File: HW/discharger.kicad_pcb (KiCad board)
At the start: 2 copper layers, 53.9 x 33.4 mm, 15 parts, among them J1 Conn_01x04_Male, J2 Conn_01x02_Male, Q1 IRFFR220N, U1 MCP4725, U2 OP07, U3 OP07, U4 INA219

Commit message: Add files via upload
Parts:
- removed U3: OP07, Housings_DIP:DIP-8_W7.62mm_Socket_LongPads
- removed U4: INA219, TO_SOT_Packages_SMD:SOT-23-8_Handsoldering
- added 1U1: 0,1U, Capacitors_SMD:C_0805_HandSoldering, F.Cu at (333.5, 75.7)
- added 1U2: 0,1U, Capacitors_SMD:C_0805_HandSoldering, F.Cu at (325.8, 84.5)
- added C10: 100n, Capacitors_SMD:C_0805_HandSoldering, F.Cu at (228.1, 115.7)
- added C11: 100n, Capacitors_SMD:C_0805_HandSoldering, F.Cu at (233.1, 115.7)
- added C12: 100n, Capacitors_SMD:C_0805_HandSoldering, F.Cu at (290.9, 72.5)
- added C13: C, Capacitors_SMD:C_0805_HandSoldering, F.Cu at (265.3, 94.9)
- added C14: C, Capacitors_SMD:C_0805_HandSoldering, F.Cu at (283.9, 76.8)
- added C15: 100n, Capacitors_SMD:C_0805_HandSoldering, F.Cu at (270.2, 97.9)
- added C18: 100n, Capacitors_SMD:C_0805_HandSoldering, F.Cu at (265.3, 100.4)
- added C19: C, Capacitors_SMD:C_0805_HandSoldering, F.Cu at (288.8, 78.0)
- added C20: 0,1u, Capacitors_SMD:C_0805_HandSoldering, F.Cu at (344.8, 65.8)
- added C21: 10uF, Capacitors_Tantalum_SMD:CP_Tantalum_Case-C_EIA-6032-28_Hand, F.Cu at (329.7, 67.4)
- added C22: 0,1U, Capacitors_SMD:C_0805_HandSoldering, F.Cu at (349.7, 65.8)
- added C23: 22pf, Capacitors_SMD:C_0805_HandSoldering, F.Cu at (344.8, 71.3)
- added C24: 22pf, Capacitors_SMD:C_0805_HandSoldering, F.Cu at (330.7, 84.5)
- added C25: 100nF, Capacitors_SMD:C_0805_HandSoldering, F.Cu at (236.7, 126.4)
- added C26: 100nF, Capacitors_SMD:C_0805_HandSoldering, F.Cu at (253.4, 128.4)
- added C27: 100nF, Capacitors_SMD:C_0805_HandSoldering, F.Cu at (242.1, 140.2)
- added C7: C, Capacitors_SMD:C_0805_HandSoldering, F.Cu at (305.2, 119.7)
- added C8: C, Capacitors_SMD:C_0805_HandSoldering, F.Cu at (316.0, 102.2)
- added C9: 100n, Capacitors_SMD:C_0805_HandSoldering, F.Cu at (242.1, 88.8)
- added D1: LED1, LEDs:LED_D5.0mm-4, F.Cu at (317.9, 82.3)
- added D2: LED2, LEDs:LED_D5.0mm-4, F.Cu at (325.7, 76.7)
- added D3: LED3, LEDs:LED_D5.0mm-4, F.Cu at (336.9, 68.0)
- added FTDI1: FTDI, Pin_Headers:Pin_Header_Straight_1x06_Pitch2.54mm, F.Cu at (299.2, 80.5)
- added ISP1: ISP-header, Pin_Headers:Pin_Header_Straight_2x03_Pitch2.54mm, F.Cu at (310.5, 89.6)
- added J3: Batt1, Connectors_Terminal_Blocks:TerminalBlock_bornier-2_P5.08mm, F.Cu at (210.7, 127.4)
- added J4: Batt1, Connectors_Terminal_Blocks:TerminalBlock_bornier-2_P5.08mm, F.Cu at (204.6, 95.5)
- added JP1: Jumper, Pin_Headers:Pin_Header_Straight_1x03_Pitch2.54mm, F.Cu at (304.3, 89.6)
- added Q2: IRFFR220N, TO_SOT_Packages_SMD:TO-252-2, F.Cu at (192.4, 130.1)
- added Q3: IRFFR220N, TO_SOT_Packages_SMD:TO-252-2, F.Cu at (180.5, 103.4)
- added Q4: FS8205, TO_SOT_Packages_SMD:SOT-23-6_Handsoldering, F.Cu at (178.2, 67.1)
- added Q5: FS8205, TO_SOT_Packages_SMD:SOT-23-6_Handsoldering, F.Cu at (207.7, 118.6)
- added Q6: FS8205, TO_SOT_Packages_SMD:SOT-23-6_Handsoldering, F.Cu at (179.2, 73.7)
- added R10: 1K, Resistors_SMD:R_0805_HandSoldering, F.Cu at (349.8, 71.3)
- added R11: 1K, Resistors_SMD:R_0805_HandSoldering, F.Cu at (338.6, 75.7)
- added R12: 100R, Resistors_SMD:R_0805_HandSoldering, F.Cu at (244.5, 123.4)
- added R13: 100R, Resistors_SMD:R_0805_HandSoldering, F.Cu at (252.4, 143.3)
- added R14: 1K, Resistors_SMD:R_0805_HandSoldering, F.Cu at (242.1, 136.1)
- added R15: 1K, Resistors_SMD:R_0805_HandSoldering, F.Cu at (252.4, 137.8)
- added R16: 100R, Resistors_SMD:R_0805_HandSoldering, F.Cu at (247.2, 143.3)
- added R17: 1K, Resistors_SMD:R_0805_HandSoldering, F.Cu at (244.4, 147.3)
- added R18: R, Resistors_SMD:R_0805_HandSoldering, F.Cu at (343.7, 82.3)
- added R19: R, Resistors_SMD:R_0805_HandSoldering, F.Cu at (338.6, 81.2)
- added R20: R, Resistors_SMD:R_0805_HandSoldering, F.Cu at (355.0, 71.2)
- added R21: R, Resistors_SMD:R_0805_HandSoldering, F.Cu at (336.6, 86.7)
- added R22: R, Resistors_SMD:R_0805_HandSoldering, F.Cu at (349.8, 76.8)
- added R23: R, Resistors_SMD:R_0805_HandSoldering, F.Cu at (326.3, 95.5)
- added R24: R, Resistors_SMD:R_0805_HandSoldering, F.Cu at (331.4, 90.0)
- added R25: R, Resistors_SMD:R_0805_HandSoldering, F.Cu at (343.7, 76.8)
- added R26: R, Resistors_SMD:R_0805_HandSoldering, F.Cu at (354.8, 65.7)
- added R3: 0,01R, Resistors_SMD:R_2512_HandSoldering, F.Cu at (194.5, 90.3)
- added R4: 10R, Resistors_THT:R_Axial_DIN0414_L11.9mm_D4.5mm_P15.24mm_Horizontal, F.Cu at (148.6, 109.6)
- added R5: 0,01R, Resistors_SMD:R_2512_HandSoldering, F.Cu at (202.1, 129.7)
- added R6: 10R, Resistors_THT:R_Axial_DIN0414_L11.9mm_D4.5mm_P15.24mm_Horizontal, F.Cu at (184.4, 132.8)
- added R7: 0,01R, Resistors_SMD:R_2512_HandSoldering, F.Cu at (194.3, 100.9)
- added R8: 10R, Resistors_THT:R_Axial_DIN0414_L11.9mm_D4.5mm_P15.24mm_Horizontal, F.Cu at (137.9, 124.8)
- added R9: 10K, Resistors_SMD:R_0805_HandSoldering, F.Cu at (326.3, 90.0)
- added TP3: TEST, Pin_Headers:Pin_Header_Straight_1x01_Pitch2.54mm, F.Cu at (243.8, 45.9)
- added U12: OP07, Housings_DIP:DIP-8_W7.62mm_Socket_LongPads, F.Cu at (248.9, 80.7)
- added U13: INA219, TO_SOT_Packages_SMD:SOT-23-8_Handsoldering, F.Cu at (126.5, 81.6)
- added U14: ATMEGA328P-AU-Arduino, Housings_QFP:TQFP-32_7x7mm_Pitch0.8mm, F.Cu at (306.9, 70.1)
- added U15: DW01-P, TO_SOT_Packages_SMD:SOT-23-6_Handsoldering, F.Cu at (162.4, 66.6)
- added U16: DW01-P, TO_SOT_Packages_SMD:SOT-23-6_Handsoldering, F.Cu at (203.3, 118.5)
- added U17: DW01-P, TO_SOT_Packages_SMD:SOT-23-6_Handsoldering, F.Cu at (169.2, 66.4)
- added U6: OP07, Housings_DIP:DIP-8_W7.62mm_Socket_LongPads, F.Cu at (219.1, 83.7)
- added U7: OP07, Housings_DIP:DIP-8_W7.62mm_Socket_LongPads, F.Cu at (224.5, 67.3)
- added U8: INA219, TO_SOT_Packages_SMD:SOT-23-8_Handsoldering, F.Cu at (126.5, 94.5)
- added U9: INA219, TO_SOT_Packages_SMD:SOT-23-8_Handsoldering, F.Cu at (126.4, 88.2)
- added Y1: 8MHZ, Crystals:Crystal_HC18-U_Vertical, F.Cu at (305.2, 81.7)
- C1: value C -> 10uF; footprint Capacitors_SMD:C_0805_HandSoldering -> Capacitors_Tantalum_SMD:CP_Tantalum_Case-C_EIA-6032-28_Hand
- C2: value C -> 2uF
- C3: value C -> 100uF; footprint Capacitors_SMD:C_0805_HandSoldering -> Capacitors_THT:CP_Radial_D6.3mm_P2.50mm
- C4: value C -> 2nF
- J1: value Conn_01x04_Male -> OLED; footprint Pin_Headers:Pin_Header_Straight_1x04_Pitch2.54mm_SMD_Pin1Right -> Pin_Headers:Pin_Header_Straight_1x04_Pitch2.54mm_SMD_Pin1Left
- J2: value Conn_01x02_Male -> Batt1; footprint Pin_Headers:Pin_Header_Straight_1x02_Pitch2.54mm_SMD_Pin1Right -> Connectors_Terminal_Blocks:TerminalBlock_bornier-2_P5.08mm
- R1: value 0,01R -> 20K; footprint Resistors_SMD:R_2512_HandSoldering -> Resistors_SMD:R_0805_HandSoldering
- R2: value 10R -> 102.6K; footprint Resistors_THT:R_Axial_DIN0414_L11.9mm_D4.5mm_P15.24mm_Horizontal -> Resistors_SMD:R_0805_HandSoldering
- U1: value MCP4725 -> LT1054; footprint TO_SOT_Packages_SMD:SOT-23-6_Handsoldering -> Housings_DIP:DIP-8_W7.62mm_LongPads
- U2: value OP07 -> MCP4728; footprint Housings_DIP:DIP-8_W7.62mm_Socket_LongPads -> Housings_SSOP:MSOP-10_3x3mm_Pitch0.5mm
- moved C4 168.3 mm to (326.7, 105.4), turned to 0 degrees
- moved C1 164.3 mm to (313.6, 107.0), turned to 0 degrees
- moved C2 162.2 mm to (321.7, 110.9), turned to 0 degrees
- moved U1 145.5 mm to (298.7, 105.9), turned to 0 degrees
- moved R1 145.1 mm to (326.8, 110.9), turned to 0 degrees
- moved U2 144.3 mm to (320.0, 90.9), turned to 0 degrees
- moved C3 129.5 mm to (310.5, 116.8), turned to 0 degrees
- moved J1 128.3 mm to (320.4, 70.2), turned to 0 degrees
- moved R2 124.0 mm to (299.9, 119.6)
- moved TP1 81.8 mm to (239.1, 46.0)
- moved TP2 80.1 mm to (235.5, 46.4)
- moved J2 13.1 mm to (204.6, 84.9), turned to 270 degrees
- moved Q1 5.27 mm to (180.4, 93.7), turned to 180 degrees
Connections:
- C1 pad 1: VCC -> Net-(C1-Pad1)
- C1 pad 2: GND -> Net-(C1-Pad2)
- C3 pad 1: VCC -> GND
- C3 pad 2: GND -> -5V
- C4 pad 1: VCC -> Net-(C4-Pad1)
- C4 pad 2: GND -> -5V
- J1 pad 1: VCC -> SDA
- J1 pad 2: SDA -> SCL
- J1 pad 3: SCL -> VCC
- J2 pad 1: GND -> Net-(C25-Pad2)
- J2 pad 2: Net-(J2-Pad2) -> /Battery connections/BatteryPositive1
- R1 pad 1: Net-(J2-Pad2) -> Net-(C4-Pad1)
- R1 pad 2: Net-(Q1-Pad2) -> Net-(R1-Pad2)
- R2 pad 1: Net-(Q1-Pad3) -> Net-(C4-Pad1)
- R2 pad 2: GND -> -5V
- TP1 pad 1: Net-(TP1-Pad1) -> /Dynamic load/DAC_IN1
- TP2 pad 1: Net-(TP2-Pad1) -> /Dynamic load/DAC_IN3
- U1 pad 1: Net-(TP2-Pad1) -> Net-(C4-Pad1)
- U1 pad 2: GND -> Net-(C1-Pad1)
- U1 pad 3: VCC -> GND
- U1 pad 4: SDA -> Net-(C1-Pad2)
- U1 pad 5: SCL -> -5V
- U1 pad 6: GND -> Net-(R1-Pad2)
- U2 pad 1: (no net) -> VCC
- U2 pad 2: Net-(TP1-Pad1) -> SCL
- U2 pad 3: Net-(J2-Pad2) -> SDA
- U2 pad 6: Net-(TP1-Pad1) -> /Dynamic load/DAC_IN1
- U2 pad 7: VCC -> /Dynamic load/DAC_IN2
- U2 pad 8: (no net) -> /Dynamic load/DAC_IN3
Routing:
- net VCC: track 83.0 -> 0.00 mm
- net SDA: track 65.9 -> 0.00 mm
- net SCL: track 59.8 -> 0.00 mm
- net GND: track 46.7 -> 0.00 mm
- net Net-(J2-Pad2): track 31.2 -> 0.00 mm
- net Net-(TP2-Pad1): track 27.1 -> 0.00 mm
- net Net-(Q1-Pad3): track 26.1 -> 0.00 mm
- net Net-(Q1-Pad1): track 16.9 -> 0.00 mm
- net Net-(TP1-Pad1): track 16.1 -> 0.00 mm
- net /Battery connections/BatteryPositive3: track 0.00 -> 14.0 mm
- net Net-(Q2-Pad2): track 0.00 -> 12.5 mm
- net Net-(C26-Pad2): track 0.00 -> 12.5 mm
- net Net-(Q2-Pad3): track 0.00 -> 11.3 mm
- net Net-(Q1-Pad2): track 11.0 -> 0.00 mm
- net Net-(Q5-Pad4): track 0.00 -> 9.79 mm
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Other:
- board size 53.9 x 33.4 mm -> 96.1 x 73.7 mm

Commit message: Add files via upload
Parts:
- removed C24: 22pf, Capacitors_SMD:C_0805_HandSoldering
- removed C25, C26, C27: 100nF, Capacitors_SMD:C_0805_HandSoldering
- removed ISP1: ISP-header, Pin_Headers:Pin_Header_Straight_2x03_Pitch2.54mm
- removed U14: ATMEGA328P-AU-Arduino, Housings_QFP:TQFP-32_7x7mm_Pitch0.8mm
- removed U15, U16, U17: DW01-P, TO_SOT_Packages_SMD:SOT-23-6_Handsoldering
- added C16: 10uF, Capacitors_Tantalum_SMD:CP_Tantalum_Case-C_EIA-6032-28_Hand, B.Cu at (274.0, 109.7)
- added C17: 0,1u, Capacitors_SMD:C_0805_HandSoldering, B.Cu at (245.4, 117.2)
- added C5: 2nF, Capacitors_SMD:C_0805_HandSoldering, B.Cu at (151.1, 72.1)
- added C6: 100uF, Capacitors_THT:CP_Radial_D6.3mm_P2.50mm, F.Cu at (168.8, 70.9)
- added J5: Batt1, Connectors_Terminal_Blocks:TerminalBlock_bornier-2_P5.08mm, B.Cu at (126.9, 132.0)
- added U10: MCP4728, Housings_SSOP:MSOP-10_3x3mm_Pitch0.5mm, B.Cu at (228.8, 80.5)
- added U11: DW01-P, TO_SOT_Packages_SMD:SOT-23-6_Handsoldering, F.Cu at (132.2, 103.8)
- added U3: INA219, TO_SOT_Packages_SMD:SOT-23-8_Handsoldering, F.Cu at (145.3, 107.2)
- added U4: INA219, TO_SOT_Packages_SMD:SOT-23-8_Handsoldering, F.Cu at (144.7, 82.8)
- added U5: OP07, Housings_DIP:DIP-8_W7.62mm_Socket_LongPads, F.Cu at (175.9, 108.3)
- 1U1, 1U2, C11, C12, C15, D1, D2, D3, J3, J4, R1, R10, R11, R18, R19, R2, R20, R9, Y1: moved to B.Cu
- C1: value 10uF -> 2uF; footprint Capacitors_Tantalum_SMD:CP_Tantalum_Case-C_EIA-6032-28_Hand -> Capacitors_SMD:C_0805_HandSoldering; moved to B.Cu
- C14: value C -> 100n
- C18: value 100n -> 22pf; moved to B.Cu
- C19: value C -> 0,1U; moved to B.Cu
- C2: value 2uF -> 10uF; footprint Capacitors_SMD:C_0805_HandSoldering -> Capacitors_Tantalum_SMD:CP_Tantalum_Case-C_EIA-6032-28_Hand; moved to B.Cu
- C20: value 0,1u -> 22pf; moved to B.Cu
- C21: value 10uF -> 100nF; footprint Capacitors_Tantalum_SMD:CP_Tantalum_Case-C_EIA-6032-28_Hand -> Capacitors_SMD:C_0805_HandSoldering
- C22: value 0,1U -> 100nF
- C23: value 22pf -> 100nF
- C3: value 100uF -> 10uF; footprint Capacitors_THT:CP_Radial_D6.3mm_P2.50mm -> Capacitors_SMD:C_0805_HandSoldering; moved to B.Cu
- C4: value 2nF -> 0,1uF; moved to B.Cu
- J1: value OLED -> Vin; footprint Pin_Headers:Pin_Header_Straight_1x04_Pitch2.54mm_SMD_Pin1Left -> Connectors_Terminal_Blocks:TerminalBlock_bornier-2_P5.08mm; moved to B.Cu
- J2: value Batt1 -> OLED; footprint Connectors_Terminal_Blocks:TerminalBlock_bornier-2_P5.08mm -> Pin_Headers:Pin_Header_Straight_1x04_Pitch2.54mm_SMD_Pin1Left; moved to B.Cu
- Q4, Q5, Q6: value FS8205 -> IRF7341; footprint TO_SOT_Packages_SMD:SOT-23-6_Handsoldering -> Housings_SOIC:SO-8_5.3x6.2mm_Pitch1.27mm
- R12, R13, R16: value 100R -> R; moved to B.Cu
- R14, R15, R17: value 1K -> R; moved to B.Cu
- R21, R22, R25: value R -> 100R
- R23, R24, R26: value R -> 1K
- R4: value 10R -> 0,01R; footprint Resistors_THT:R_Axial_DIN0414_L11.9mm_D4.5mm_P15.24mm_Horizontal -> Resistors_SMD:R_2512_HandSoldering
- R5: value 0,01R -> 10R; footprint Resistors_SMD:R_2512_HandSoldering -> Resistors_THT:R_Axial_DIN0414_L11.9mm_D4.5mm_P15.24mm_Horizontal
- U1: value LT1054 -> LM2937; footprint Housings_DIP:DIP-8_W7.62mm_LongPads -> TO_SOT_Packages_SMD:SOT-223-3_TabPin2; moved to B.Cu
- U12: value OP07 -> DW01-P; footprint Housings_DIP:DIP-8_W7.62mm_Socket_LongPads -> TO_SOT_Packages_SMD:SOT-23-6_Handsoldering
- U13: value INA219 -> DW01-P; footprint TO_SOT_Packages_SMD:SOT-23-8_Handsoldering -> TO_SOT_Packages_SMD:SOT-23-6_Handsoldering
- U2: value MCP4728 -> LT1054; footprint Housings_SSOP:MSOP-10_3x3mm_Pitch0.5mm -> Housings_DIP:DIP-8_W7.62mm_LongPads
- U7: value OP07 -> INA219; footprint Housings_DIP:DIP-8_W7.62mm_Socket_LongPads -> TO_SOT_Packages_SMD:SOT-23-8_Handsoldering
- U8: value INA219 -> OP07; footprint TO_SOT_Packages_SMD:SOT-23-8_Handsoldering -> Housings_DIP:DIP-8_W7.62mm_Socket_LongPads
- U9: value INA219 -> ATMEGA328P-AU-Arduino; footprint TO_SOT_Packages_SMD:SOT-23-8_Handsoldering -> Housings_QFP:TQFP-32_7x7mm_Pitch0.8mm; moved to B.Cu
- moved R26 233.2 mm to (128.3, 121.0), turned to 90 degrees
- moved R25 228.1 mm to (122.6, 132.6), turned to 270 degrees
- moved C23 227.9 mm to (123.7, 126.7), turned to 270 degrees
- moved C22 219.2 mm to (130.8, 76.2), turned to 180 degrees
- moved R22 219.0 mm to (130.8, 73.7), turned to 180 degrees
- moved R21 206.0 mm to (130.8, 97.4), turned to 180 degrees
- moved C21 201.6 mm to (130.8, 99.9), turned to 180 degrees
- moved J1 196.1 mm to (124.3, 67.2)
- moved R24 194.8 mm to (136.9, 80.0)
- moved C4 194.2 mm to (135.6, 71.1), turned to 90 degrees
- moved R23 189.8 mm to (136.7, 103.8)
- moved R1 184.8 mm to (146.2, 72.0), turned to 90 degrees
- moved C3 176.1 mm to (140.4, 71.1), turned to 90 degrees
- moved C1 168.9 mm to (150.1, 64.8), turned to 180 degrees
- moved C8 167.4 mm to (149.5, 84.3)
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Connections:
- C1 pad 1: Net-(C1-Pad1) -> VCC
- C1 pad 2: Net-(C1-Pad2) -> GND
- C11 pad 1: VCC -> GND
- C12 pad 1: VCC -> GND
- C15 pad 1: VCC -> GND
- C15 pad 2: GND -> -5V
- C18 pad 1: VCC -> GND
- C18 pad 2: -5V -> Net-(C18-Pad2)
- C19 pad 1: VCC -> Net-(C19-Pad1)
- C2 pad 1: VCC -> Net-(C2-Pad1)
- C2 pad 2: GND -> Net-(C2-Pad2)
- C20 pad 1: RST -> GND
- C20 pad 2: reset_in -> Net-(C20-Pad2)
- C21 pad 1: VCC -> Net-(C21-Pad1)
- C21 pad 2: GND -> Net-(C21-Pad2)
- C22 pad 2: GND -> Net-(C22-Pad2)
- C23 pad 1: GND -> Net-(C23-Pad1)
- C3 pad 1: GND -> VCC
- C3 pad 2: -5V -> GND
- C4 pad 2: -5V -> GND
- C7 pad 1: (no net) -> VCC
- C7 pad 2: (no net) -> GND
- C8 pad 1: (no net) -> VCC
- C8 pad 2: (no net) -> GND
- J1 pad 1: SDA -> GND
- J1 pad 2: SCL -> Net-(C4-Pad1)
- J2 pad 1: Net-(C25-Pad2) -> SDA
- J2 pad 2: /Battery connections/BatteryPositive1 -> SCL
- J3 pad 1: Net-(C26-Pad2) -> Net-(C21-Pad2)
- J3 pad 2: /Battery connections/BatteryPositive3 -> /Battery connections/BatteryPositive1
- J4 pad 1: Net-(C27-Pad2) -> Net-(C22-Pad2)
- Q4 pad 1: Net-(C25-Pad2) -> GND
- Q4 pad 3: GND -> Net-(C21-Pad2)
- Q4 pad 5: Net-(Q4-Pad2) -> Net-(Q4-Pad5)
- Q4 pad 6: Net-(Q4-Pad6) -> (no net)
- Q5 pad 1: Net-(C26-Pad2) -> GND
- Q5 pad 3: GND -> Net-(C22-Pad2)
- Q5 pad 5: Net-(Q5-Pad2) -> Net-(Q5-Pad5)
- Q5 pad 6: Net-(Q5-Pad6) -> (no net)
- Q6 pad 1: Net-(C27-Pad2) -> GND
- Q6 pad 3: GND -> Net-(C23-Pad2)
- Q6 pad 5: Net-(Q6-Pad2) -> Net-(Q6-Pad5)
- Q6 pad 6: Net-(Q6-Pad6) -> (no net)
- R1 pad 1: Net-(C4-Pad1) -> Net-(C5-Pad1)
- R12 pad 1: Net-(C25-Pad1) -> Net-(D1-Pad1)
- R12 pad 2: /Battery connections/BatteryPositive1 -> Led1R
- R13 pad 1: Net-(C26-Pad1) -> Net-(D2-Pad1)
- R13 pad 2: /Battery connections/BatteryPositive3 -> Led2R
- R14 pad 1: Net-(R14-Pad1) -> Net-(D3-Pad1)
- R14 pad 2: GND -> Led3R
- R15 pad 1: Net-(R15-Pad1) -> Net-(D1-Pad4)
- R15 pad 2: GND -> Led1G
- R16 pad 1: Net-(C27-Pad1) -> Net-(D2-Pad4)
- R16 pad 2: /Battery connections/BatteryPositive2 -> Led2G
- R17 pad 1: Net-(R17-Pad1) -> Net-(D3-Pad4)
- R17 pad 2: GND -> Led3G
- R18 pad 1: Net-(D1-Pad1) -> Net-(D1-Pad3)
- R18 pad 2: Led1R -> Led1B
- R19 pad 1: Net-(D1-Pad4) -> Net-(D2-Pad3)
- R19 pad 2: Led1G -> Led2B
- R2 pad 1: Net-(C4-Pad1) -> Net-(C5-Pad1)
- R20 pad 1: Net-(D1-Pad3) -> Net-(D3-Pad3)
- R20 pad 2: Led1B -> Led3B
- R21 pad 1: Net-(D2-Pad1) -> Net-(C21-Pad1)
- R21 pad 2: Led2R -> /Battery connections/BatteryPositive1
- R22 pad 1: Net-(D2-Pad4) -> Net-(C22-Pad1)
- R22 pad 2: Led2G -> /Battery connections/BatteryPositive2
- R23 pad 1: Net-(D2-Pad3) -> Net-(R23-Pad1)
- R23 pad 2: Led2B -> GND
- R24 pad 1: Net-(D3-Pad1) -> Net-(R24-Pad1)
- R24 pad 2: Led3R -> GND
- R25 pad 1: Net-(D3-Pad4) -> Net-(C23-Pad1)
- R25 pad 2: Led3G -> /Battery connections/BatteryPositive3
- R26 pad 1: Net-(D3-Pad3) -> Net-(R26-Pad1)
- R26 pad 2: Led3B -> GND
- R4 pad 1: Net-(Q1-Pad3) -> /Battery connections/BatteryPositive2
- R4 pad 2: GND -> Net-(Q2-Pad2)
- R5 pad 1: /Battery connections/BatteryPositive3 -> Net-(Q1-Pad3)
- R5 pad 2: Net-(Q2-Pad2) -> GND
- R7 pad 1: /Battery connections/BatteryPositive2 -> /Battery connections/BatteryPositive3
- TP2 pad 1: /Dynamic load/DAC_IN3 -> /Dynamic load/DAC_IN2
- TP3 pad 1: /Dynamic load/DAC_IN2 -> /Dynamic load/DAC_IN3
- U1 pad 2: Net-(C1-Pad1) -> GND
- U1 pad 3: GND -> VCC
- U12 pad 1: (no net) -> Net-(Q5-Pad4)
- U12 pad 2: Net-(Q3-Pad3) -> Net-(R24-Pad1)
- U12 pad 3: /Dynamic load/DAC_IN2 -> Net-(Q5-Pad2)
- U12 pad 4: -5V -> (no net)
- U12 pad 5: (no net) -> Net-(C22-Pad1)
- U12 pad 6: Net-(Q3-Pad1) -> Net-(C22-Pad2)
- U13 pad 1: /Battery connections/BatteryPositive2 -> Net-(Q6-Pad4)
- U13 pad 2: Net-(Q3-Pad2) -> Net-(R26-Pad1)
- U13 pad 3: GND -> Net-(Q6-Pad2)
- U13 pad 4: VCC -> (no net)
- U13 pad 5: SCL -> Net-(C23-Pad1)
- U13 pad 6: SDA -> Net-(C23-Pad2)
- U2 pad 1: VCC -> Net-(C5-Pad1)
- U2 pad 2: SCL -> Net-(C2-Pad1)
- U2 pad 3: SDA -> GND
- U2 pad 4: GND -> Net-(C2-Pad2)
- U2 pad 5: (no net) -> -5V
- U2 pad 6: /Dynamic load/DAC_IN1 -> Net-(R1-Pad2)
- U2 pad 7: /Dynamic load/DAC_IN2 -> (no net)
- U2 pad 8: /Dynamic load/DAC_IN3 -> VCC
- U6 pad 2: Net-(Q1-Pad3) -> Net-(Q2-Pad3)
- U6 pad 3: /Dynamic load/DAC_IN1 -> /Dynamic load/DAC_IN2
- U6 pad 6: Net-(Q1-Pad1) -> Net-(Q2-Pad1)
- U7 pad 1: (no net) -> /Battery connections/BatteryPositive3
- U7 pad 2: Net-(Q2-Pad3) -> Net-(Q3-Pad2)
- U7 pad 3: /Dynamic load/DAC_IN3 -> GND
- U7 pad 4: -5V -> VCC
- U7 pad 5: (no net) -> SCL
- U7 pad 6: Net-(Q2-Pad1) -> SDA
- U7 pad 7: VCC -> GND
- U7 pad 8: (no net) -> GND
- U8 pad 1: /Battery connections/BatteryPositive1 -> (no net)
- U8 pad 2: Net-(Q1-Pad2) -> Net-(Q3-Pad3)
- U8 pad 3: GND -> /Dynamic load/DAC_IN3
- U8 pad 4: VCC -> -5V
- U8 pad 5: SCL -> (no net)
- U8 pad 6: SDA -> Net-(Q3-Pad1)
- U8 pad 7: SDA -> VCC
- U8 pad 8: GND -> (no net)
- U9 pad 1: /Battery connections/BatteryPositive3 -> Led3G
- U9 pad 2: Net-(Q2-Pad2) -> Led3B
- U9 pad 5: SCL -> GND
- U9 pad 6: SDA -> VCC
- U9 pad 7: GND -> Net-(C18-Pad2)
- U9 pad 8: GND -> Net-(C20-Pad2)
- Y1 pad 1: Net-(C23-Pad2) -> Net-(C18-Pad2)
- Y1 pad 2: Net-(C24-Pad2) -> Net-(C20-Pad2)
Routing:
- net VCC: track 0.00 -> 128.2 mm, vias 0 -> 3
- net -5V: track 0.00 -> 96.3 mm
- net SCL: track 0.00 -> 72.3 mm, vias 0 -> 3
- net SDA: track 0.00 -> 67.5 mm, vias 0 -> 3
- net /Battery connections/BatteryPositive2: track 0.54 -> 43.6 mm
- net /Battery connections/BatteryPositive1: track 0.36 -> 43.1 mm
- net GND: track 0.00 -> 41.9 mm
- net Net-(Q1-Pad3): track 0.00 -> 30.4 mm
- net Net-(Q3-Pad3): track 0.00 -> 29.7 mm
- net Net-(C23-Pad2): track 0.00 -> 23.6 mm
- net Net-(C22-Pad2): track 0.00 -> 21.0 mm
- net Net-(C21-Pad2): track 0.00 -> 20.6 mm
- net Net-(Q2-Pad3): track 11.3 -> 29.5 mm
- net Net-(R1-Pad2): track 0.00 -> 17.1 mm
- net Net-(Q3-Pad2): track 0.00 -> 13.3 mm
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- added copper zone on B.Cu, net GND
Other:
- net class Batt+ added: clearance 0.4, trace_width 0.8, via_dia 0.6, via_drill 0.4
- net class Default: clearance 0.2 -> 0.1; via_dia 0.6 -> 1.5; via_drill 0.4 -> 0.8
- rule trace_clearance: 0.2 -> 0.1

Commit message: Add files via upload
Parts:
- D1, D2, D3, J2, R10, R11, Y1: moved to F.Cu
- U10: footprint Housings_SSOP:MSOP-10_3x3mm_Pitch0.5mm -> Peter:MCP4728_on_a_breadboard
- moved J2 119.5 mm to (144.3, 73.2), turned to 90 degrees
- moved R18 111.0 mm to (192.7, 73.9), turned to 270 degrees
- moved R14 110.4 mm to (181.8, 73.7), turned to 270 degrees
- moved R17 110.3 mm to (187.0, 73.7), turned to 270 degrees
- moved R10 101.7 mm to (140.5, 70.6)
- moved R11 100.3 mm to (145.6, 70.5), turned to 90 degrees
- moved R15 91.8 mm to (195.2, 73.9), turned to 270 degrees
- moved R20 90.7 mm to (184.4, 73.6), turned to 270 degrees
- moved 1U1 84.1 mm to (198.2, 106.5), turned to 270 degrees
- moved 1U2 83.9 mm to (189.2, 133.9)
- moved C18 81.6 mm to (191.5, 84.9)
- moved R19 80.6 mm to (201.1, 73.8), turned to 270 degrees
- moved R12 79.9 mm to (190.1, 73.9), turned to 270 degrees
- moved R16 79.1 mm to (203.4, 73.8), turned to 270 degrees
- moved C20 77.6 mm to (197.3, 88.5), turned to 90 degrees
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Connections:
- Q4 pad 6: (no net) -> Net-(Q4-Pad5)
- Q4 pad 7: (no net) -> Net-(Q4-Pad5)
- Q5 pad 6: (no net) -> Net-(Q5-Pad5)
- Q5 pad 7: (no net) -> Net-(Q5-Pad5)
- Q6 pad 6: (no net) -> Net-(Q6-Pad5)
- Q6 pad 7: (no net) -> Net-(Q6-Pad5)
- U9 pad 1: Led3G -> Led3B
- U9 pad 10: Led1G -> Led1B
- U9 pad 11: Led1B -> Led1G
- U9 pad 13: Led2G -> Led2B
- U9 pad 14: Led2B -> Led2G
- U9 pad 2: Led3B -> Led3G
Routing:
- net VCC: track 128.2 -> 427.6 mm
- net SDA: track 67.5 -> 148.4 mm, vias 3 -> 4
- net SCL: track 72.3 -> 152.4 mm, vias 3 -> 4
- net GND: track 41.9 -> 117.0 mm
- net /Dynamic load/DAC_IN2: track 7.36 -> 70.5 mm
- net Led2G: track 0.00 -> 30.6 mm
- net Led2B: track 0.00 -> 29.7 mm
- net Led2R: track 0.00 -> 29.3 mm
- net Led1G: track 0.00 -> 28.4 mm
- net /Dynamic load/DAC_IN1: track 8.23 -> 35.9 mm
- net Led1B: track 0.00 -> 27.0 mm
- net /Dynamic load/DAC_IN3: track 8.21 -> 35.1 mm
- net Led1R: track 0.00 -> 26.8 mm
- net Led3R: track 0.00 -> 23.6 mm
- net Led3B: track 0.00 -> 21.7 mm
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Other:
- board size 96.1 x 73.7 mm -> 87.2 x 73.7 mm
- net class Default: clearance 0.1 -> 0.2
- rule trace_clearance: 0.1 -> 0.2
- board text added: "B1"
- board text added: "B2"
- board text added: "B3"
- board text added: "FTDI"
- board text added: "RST"
- board text added: "VIN"

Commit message: Add files via upload
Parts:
- moved J1 3.76 mm to (125.1, 70.9), turned to 90 degrees
- moved R22 2.58 mm to (133.3, 74.1)
- moved C7 2.25 mm to (148.4, 107.1), turned to 90 degrees
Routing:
- net GND: track 117.0 -> 141.7 mm, vias 0 -> 2
- net Net-(Q2-Pad3): track 43.3 -> 29.9 mm
- net Net-(C4-Pad1): track 12.4 -> 19.7 mm
- net Net-(Q1-Pad3): track 36.5 -> 30.1 mm
- net Net-(Q3-Pad3): track 36.6 -> 30.3 mm
- net SDA: track 148.4 -> 152.4 mm
- net Net-(Q1-Pad1): track 10.3 -> 13.9 mm
- net Net-(Q2-Pad1): track 13.6 -> 10.5 mm
- net SCL: track 152.4 -> 155.5 mm
- net /Battery connections/BatteryPositive2: track 43.6 -> 45.9 mm
- net Net-(C22-Pad1): track 5.23 -> 6.77 mm
- net VCC: track 427.6 -> 428.9 mm
- net Net-(Q3-Pad1): track 11.0 -> 10.1 mm
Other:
- board text removed: "VIN"

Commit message: Less bad
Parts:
- C1: moved to F.Cu
- moved R25 11.1 mm to (123.7, 121.6), turned to 90 degrees
- moved C10 8.47 mm to (172.3, 96.3), turned to 180 degrees
- moved C1 2.79 mm to (151.4, 67.2), turned to 270 degrees
- moved C19 1.83 mm to (194.4, 106.8), turned to 270 degrees
- moved R8 1.11 mm to (149.3, 119.5)
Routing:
- net VCC: track 428.9 -> 398.4 mm
- net /Battery connections/BatteryPositive3: track 25.1 -> 40.0 mm
- net GND: track 141.7 -> 156.2 mm, vias 2 -> 3
- net Net-(C4-Pad1): track 19.7 -> 24.7 mm
- net Net-(C23-Pad1): track 10.7 -> 5.81 mm
- net /Dynamic load/DAC_IN1: track 35.9 -> 38.7 mm
- net Net-(Q2-Pad3): track 29.9 -> 32.4 mm
- net Net-(Q1-Pad3): track 30.1 -> 32.0 mm
- net Net-(Q3-Pad3): track 30.3 -> 31.9 mm
- net Net-(C19-Pad1): track 4.22 -> 3.32 mm
- net /Battery connections/BatteryPositive2: track 45.9 -> 45.1 mm
- net -5V: track 97.2 -> 96.5 mm

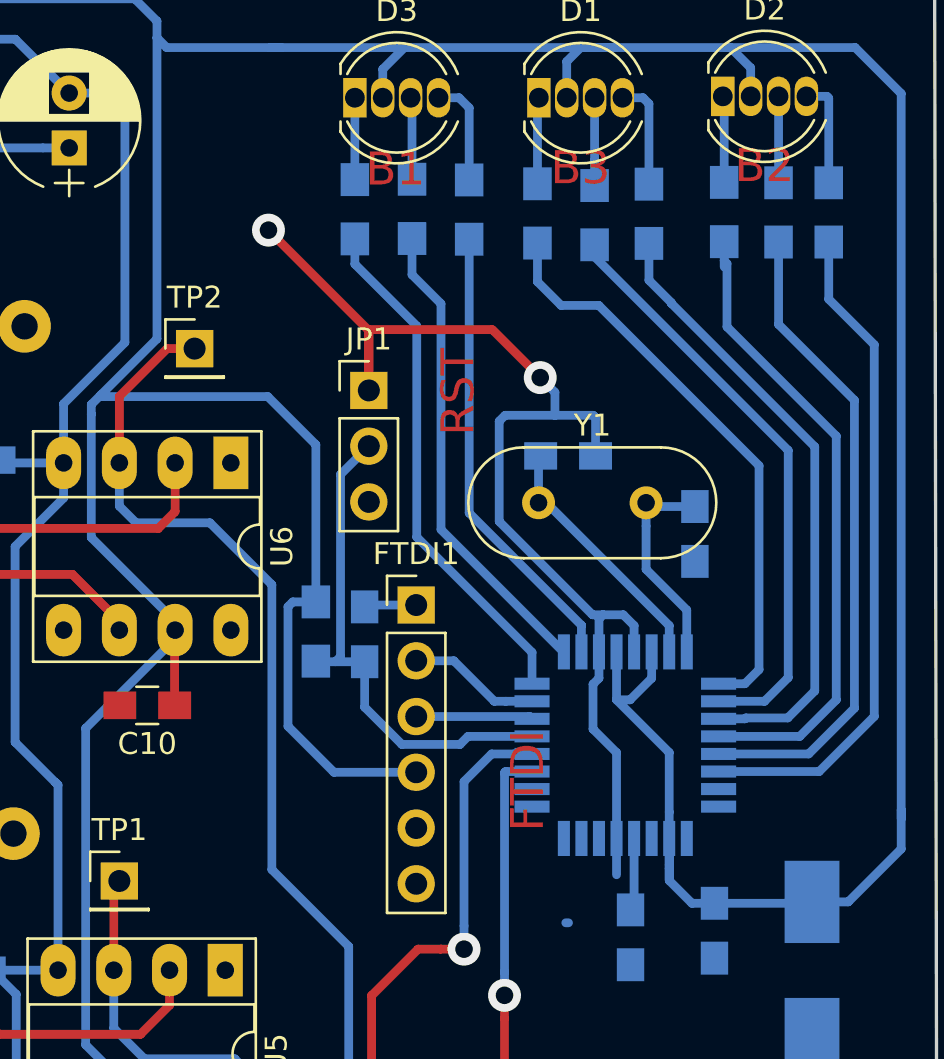
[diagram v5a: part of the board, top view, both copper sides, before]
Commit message: SMD crystal
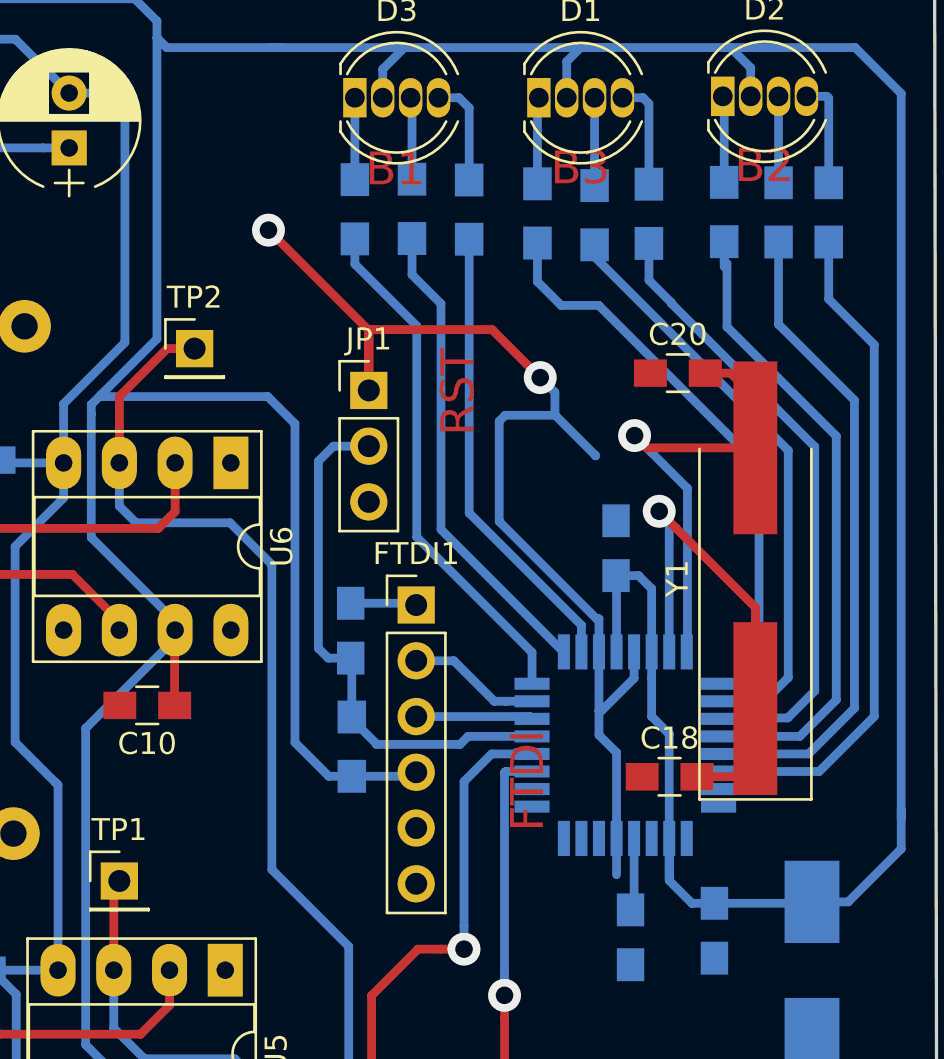
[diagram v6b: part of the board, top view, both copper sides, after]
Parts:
- added 1U1: 0,1U, Capacitors_SMD:C_0805_HandSoldering, B.Cu at (193.7, 89.1)
- C18, C20: moved to F.Cu
- Y1: footprint Crystals:Crystal_HC18-U_Vertical -> Crystals:Crystal_SMD_HC49-SD_HandSoldering
- moved C18 15.3 mm to (196.1, 99.5), turned to 0 degrees
- moved Y1 10.5 mm to (200.1, 90.5), turned to 90 degrees
- moved C20 7.37 mm to (196.5, 81.1), turned to 0 degrees
- moved R9 5.50 mm to (181.7, 98.1), turned to 90 degrees
- moved C17 0.66 mm to (181.6, 92.9)
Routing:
- net Net-(C18-Pad2): track 12.1 -> 24.6 mm, vias 0 -> 1
- net Net-(C20-Pad2): track 9.86 -> 21.6 mm, vias 0 -> 1
- net VCC: track 398.4 -> 401.5 mm
- net reset_in: track 23.2 -> 24.4 mm
- net GND: track 156.2 -> 155.1 mm
- net RST: track 2.47 -> 3.11 mm
- net /Dynamic load/DAC_IN2: track 70.5 -> 71.1 mm
